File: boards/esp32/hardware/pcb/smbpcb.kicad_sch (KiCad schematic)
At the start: 61 parts, among them IC1 MiCS-6814, J1 USB_B_Micro, J2 PMS7003, Q1 SUD08P06-155L, SW1 RESET, SW2 RESET, U1 MCP73831-2-OT, U2 SGM6603-5.0YN6G_TR, U3 ESP32-WROOM-32, U4 SSD1306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

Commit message: moving stuff
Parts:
- added D2: LED_BLUE, Capacitor_SMD:C_0805_2012Metric, symbol Device:LED
- added D6: LED_GREEN, Capacitor_SMD:C_0805_2012Metric, symbol Device:LED
- added R11, R12: 1k5, symbol Device:R
- SW1, SW2: mfr_part_num ST-1102W-4.3 -> (none)
- U4: footprint mics:SSD1306_OLED-0.91-128x32 -> stuff:SSD1306_OLED-0.91-128x32
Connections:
- net GND: now also R11.1, R12.1
- net LED_GREEN: now reaches U3.30 (IO18)
- net LED_GREEN: now also D6.2 (A)
- net LED_BLUE: now reaches U3.31 (IO19)
- net LED_BLUE: now also D2.2 (A)
- new net: D2.1 (K), R11.2
- new net: D6.1 (K), R12.2
- no-connect marks 26 -> 24
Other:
- moved on the sheet: U6

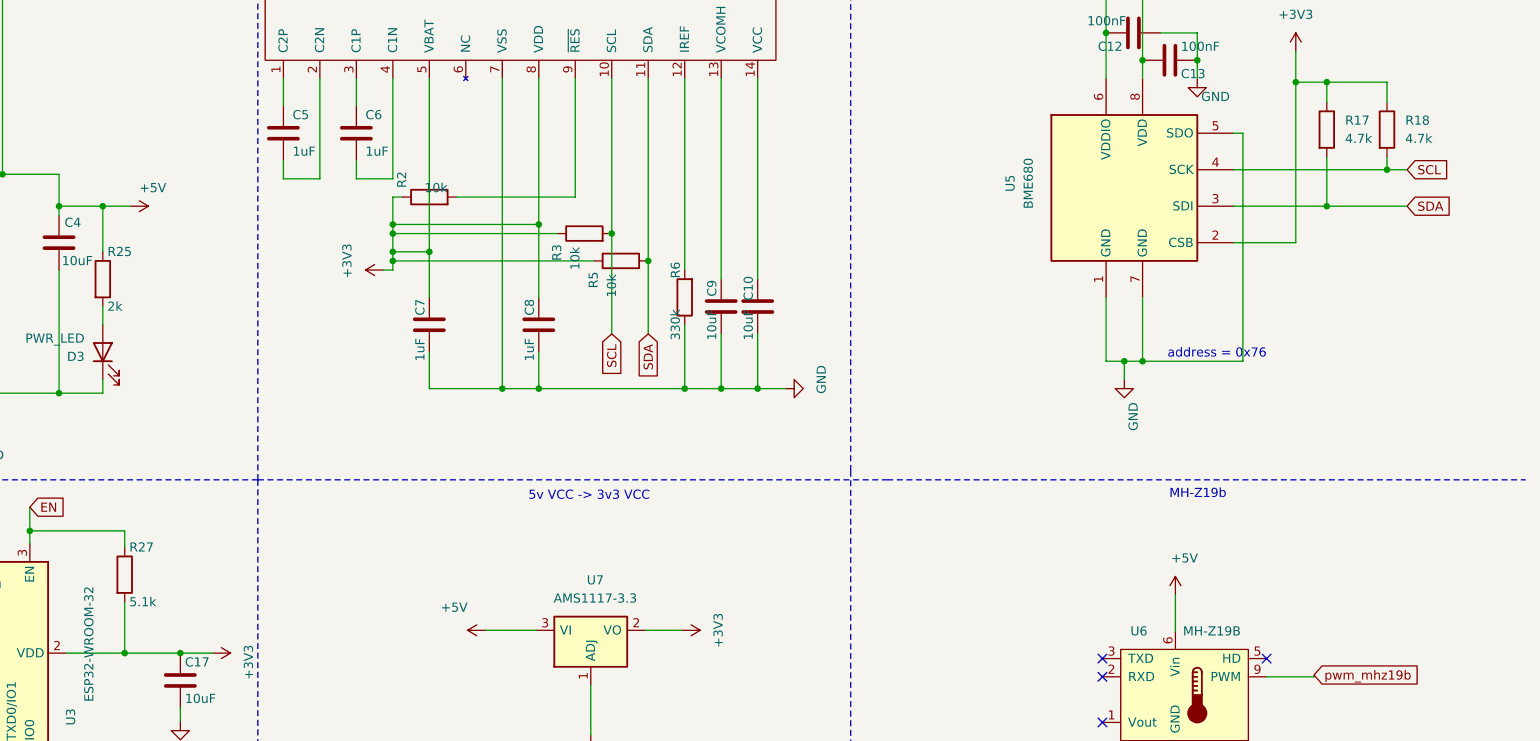
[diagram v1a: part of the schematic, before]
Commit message: added status leds
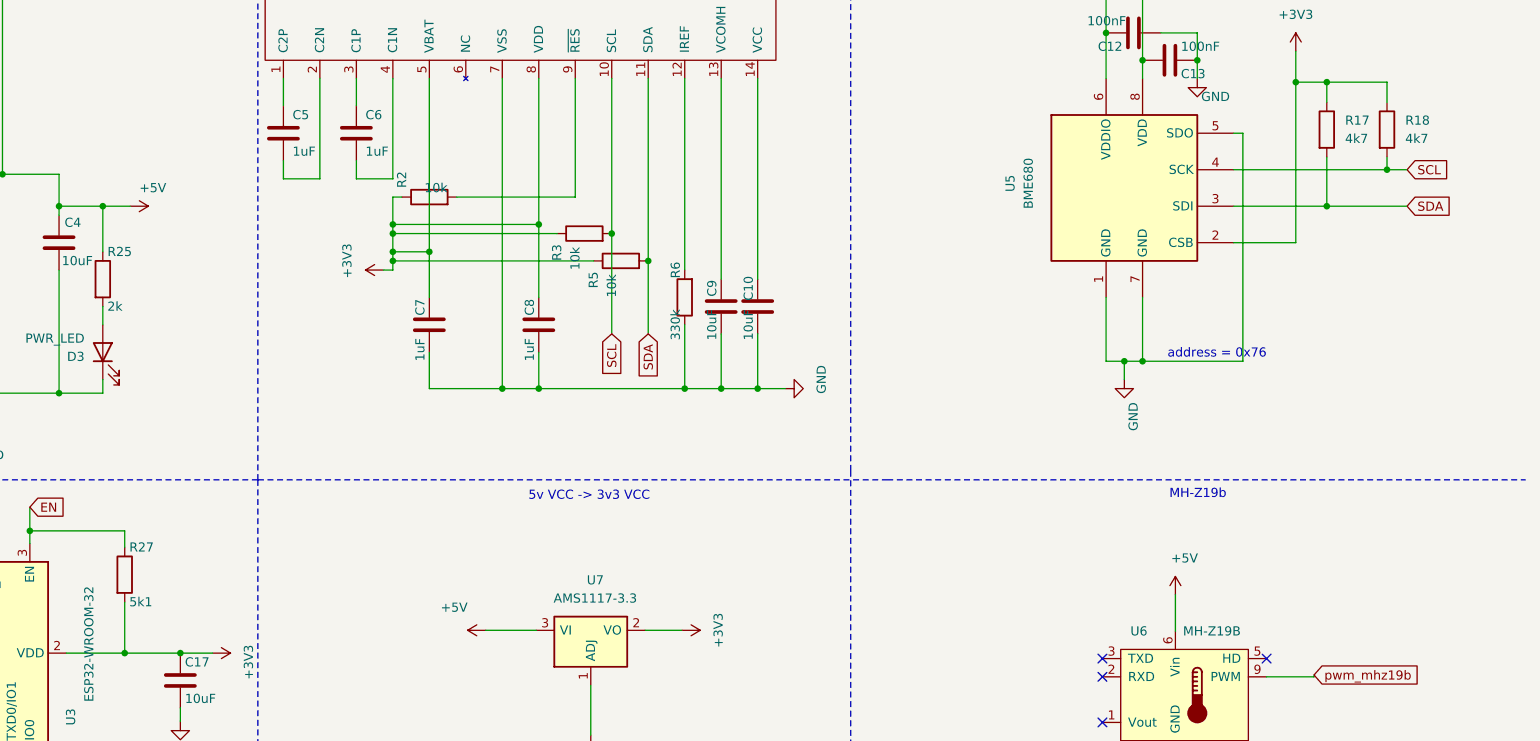
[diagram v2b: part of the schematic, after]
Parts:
- R11, R12: footprint (none) -> Capacitor_SMD:C_0805_2012Metric; LCSC (none) -> C203762; Mouser (none) -> CR0805-FX-1501ELF
- R17, R18: value 4.7k -> 4k7
- R27: value 5.1k -> 5k1
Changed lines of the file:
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@@
     (property "Reference" "R11" (id 0) (at 72.898 140.97 90))
     (property "Value" "1k5" (id 1) (at 71.247 137.922 90))
-    (property "Footprint" "" (id 2) (at 75.311 140.589 90)
+    (property "Footprint" "Capacitor_SMD:C_0805_2012Metric" (id 2) (at 75.311 140.589 90)
       (effects (font (size 1.27 1.27)) hide)
     )
     (property "Datasheet" "~" (id 3) (at 75.311 138.811 0)
+      (effects (font (size 1.27 1.27)) hide)
+    )
+    (property "LCSC" "C203762" (id 4) (at 75.311 138.811 0)
+      (effects (font (size 1.27 1.27)) hide)
+    )
+    (property "Mouser" "CR0805-FX-1501ELF" (id 5) (at 75.311 138.811 0)
       (effects (font (size 1.27 1.27)) hide)
     )
@@
     (property "Reference" "R12" (id 0) (at 73.025 143.764 90))
     (property "Value" "1k5" (id 1) (at 73.025 146.685 90))
-    (property "Footprint" "" (id 2) (at 76.581 146.812 90)
+    (property "Footprint" "Capacitor_SMD:C_0805_2012Metric" (id 2) (at 76.581 146.812 90)
       (effects (font (size 1.27 1.27)) hide)
     )
     (property "Datasheet" "~" (id 3) (at 76.581 145.034 0)
+      (effects (font (size 1.27 1.27)) hide)
+    )
+    (property "LCSC" "C203762" (id 4) (at 76.581 145.034 0)
+      (effects (font (size 1.27 1.27)) hide)
+    )
+    (property "Mouser" "CR0805-FX-1501ELF" (id 5) (at 76.581 145.034 0)
       (effects (font (size 1.27 1.27)) hide)
     )
@@
       (effects (font (size 1.27 1.27)) (justify left))
     )
-    (property "Value" "5.1k" (id 1) (at 215.773 113.538 0)
+    (property "Value" "5k1" (id 1) (at 215.773 113.538 0)
       (effects (font (size 1.27 1.27)) (justify left))
     )
@@
       (effects (font (size 1.27 1.27)) (justify left))
     )
-    (property "Value" "4.7k" (id 1) (at 385.064 49.022 0)
+    (property "Value" "4k7" (id 1) (at 385.064 49.022 0)
       (effects (font (size 1.27 1.27)) (justify left))
     )
@@
       (effects (font (size 1.27 1.27)) (justify left))
     )
-    (property "Value" "4.7k" (id 1) (at 393.446 49.022 0)
+    (property "Value" "4k7" (id 1) (at 393.446 49.022 0)
       (effects (font (size 1.27 1.27)) (justify left))
     )
@@
     )
     (path "/9ff0564e-254b-4e0a-9211-8ad0add8a40b"
-      (reference "R11") (unit 1) (value "1k5") (footprint "")
+      (reference "R11") (unit 1) (value "1k5") (footprint "Capacitor_SMD:C_0805_2012Metric")
     )
     (path "/3c9fc1fe-2257-4f43-ada5-ed1c4e4f94f3"
-      (reference "R12") (unit 1) (value "1k5") (footprint "")
+      (reference "R12") (unit 1) (value "1k5") (footprint "Capacitor_SMD:C_0805_2012Metric")
     )
     (path "/48ecb9b2-9c9c-42ac-9e9f-cab25ac716a7"
-      (reference "R17") (unit 1) (value "4.7k") (footprint "Capacitor_SMD:C_0805_2012Metric")
+      (reference "R17") (unit 1) (value "4k7") (footprint "Capacitor_SMD:C_0805_2012Metric")
     )
     (path "/33b47815-c87d-4054-811e-8a180ff4b4a5"
-      (reference "R18") (unit 1) (value "4.7k") (footprint "Capacitor_SMD:C_0805_2012Metric")
+      (reference "R18") (unit 1) (value "4k7") (footprint "Capacitor_SMD:C_0805_2012Metric")
     )
     (path "/0966f30f-63a6-408e-948c-ee9c9d9c86cb"
@@
     )
     (path "/7f6c1586-2cfd-4167-bcf0-c88517a26078"
-      (reference "R27") (unit 1) (value "5.1k") (footprint "Capacitor_SMD:C_0805_2012Metric")
+      (reference "R27") (unit 1) (value "5k1") (footprint "Capacitor_SMD:C_0805_2012Metric")
     )
     (path "/b69ae685-e389-4de0-86e5-81c4fbf5127d"

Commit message: changed some title block stuff
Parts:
- AUX_CONN1, AUX_CONN2, AUX_CONN3, AUX_CONN4: Mouser (none) -> 571-9-146278-0; mfr_part_num C124413 -> (none); notes (none) -> MOUSER MALE 40 pins per unit
- EXT_BATT1: Mouser (none) -> 801-87-040-10-001101; mfr_part_num C124375 -> (none); notes (none) -> MOUSER FEMALE 40 pins per unit
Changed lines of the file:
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@@
     (title "DiyAqi Esp32 Smb pcb")
     (date "2021-02-07")
-    (rev "v0.0.5")
+    (rev "v1.0.2")
     (company "Elam Day-Friedland")
   )
@@
       (effects (font (size 1.27 1.27)) hide)
     )
-    (property "mfr_part_num" "C124375" (id 4) (at 106.045 57.15 0)
+    (property "Mouser" "801-87-040-10-001101" (id 5) (at 106.045 57.15 0)
+      (effects (font (size 1.27 1.27)) hide)
+    )
+    (property "notes" "MOUSER FEMALE 40 pins per unit" (id 6) (at 106.045 57.15 0)
       (effects (font (size 1.27 1.27)) hide)
     )
@@
       (effects (font (size 1.27 1.27)) hide)
     )
-    (property "mfr_part_num" "C124413" (id 4) (at 41.91 109.22 0)
+    (property "Mouser" " 571-9-146278-0 " (id 5) (at 41.91 109.22 0)
+      (effects (font (size 1.27 1.27)) hide)
+    )
+    (property "notes" "MOUSER MALE 40 pins per unit" (id 6) (at 41.91 109.22 0)
       (effects (font (size 1.27 1.27)) hide)
     )
@@
       (effects (font (size 1.27 1.27)) hide)
     )
-    (property "mfr_part_num" "C124413" (id 4) (at 41.91 125.73 0)
+    (property "Mouser" " 571-9-146278-0 " (id 5) (at 41.91 125.73 0)
+      (effects (font (size 1.27 1.27)) hide)
+    )
+    (property "notes" "MOUSER MALE 40 pins per unit" (id 6) (at 41.91 125.73 0)
       (effects (font (size 1.27 1.27)) hide)
     )
@@
       (effects (font (size 1.27 1.27)) hide)
     )
-    (property "mfr_part_num" "C124413" (id 4) (at 85.09 108.585 0)
+    (property "Mouser" " 571-9-146278-0 " (id 5) (at 85.09 108.585 0)
+      (effects (font (size 1.27 1.27)) hide)
+    )
+    (property "notes" "MOUSER MALE 40 pins per unit" (id 6) (at 85.09 108.585 0)
       (effects (font (size 1.27 1.27)) hide)
     )
@@
       (effects (font (size 1.27 1.27)) hide)
     )
-    (property "mfr_part_num" "C124413" (id 4) (at 85.725 127.635 0)
+    (property "Mouser" " 571-9-146278-0 " (id 5) (at 85.725 127.635 0)
+      (effects (font (size 1.27 1.27)) hide)
+    )
+    (property "notes" "MOUSER MALE 40 pins per unit" (id 6) (at 85.725 127.635 0)
       (effects (font (size 1.27 1.27)) hide)
     )

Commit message: more readable schematic
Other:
- note added: "ESP32"
- note added: "PMS7003"
- note removed: "PMS7003 (logic is 3v3, 5V is only used for fan)"
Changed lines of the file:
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@@
   (title_block
     (title "DiyAqi Esp32 Smb pcb")
-    (date "2021-02-07")
+    (date "2021-03-20")
     (rev "v1.0.2")
     (company "Elam Day-Friedland")
@@
   )
   (polyline (pts (xy 10.16 96.52) (xy 10.16 97.79))
-    (stroke (width 0) (type dash) (color 0 0 0 0))
+    (stroke (width 1) (type dash) (color 0 0 0 0))
   )
   (polyline (pts (xy 10.16 152.4) (xy 124.46 152.4))
-    (stroke (width 0) (type dash) (color 0 0 0 0))
+    (stroke (width 1) (type dash) (color 0 0 0 0))
   )
   (polyline (pts (xy 124.46 152.4) (xy 124.46 96.52))
-    (stroke (width 0) (type dash) (color 0 0 0 0))
+    (stroke (width 1) (type dash) (color 0 0 0 0))
   )
   (polyline (pts (xy 124.46 152.4) (xy 124.46 218.44))
-    (stroke (width 0) (type dash) (color 0 0 0 0))
+    (stroke (width 1) (type dash) (color 0 0 0 0))
   )
   (polyline (pts (xy 124.46 218.44) (xy 233.68 218.44))
-    (stroke (width 0) (type dash) (color 0 0 0 0))
+    (stroke (width 1) (type dash) (color 0 0 0 0))
   )
   (polyline (pts (xy 233.68 10.16) (xy 233.68 96.52))
-    (stroke (width 0) (type dash) (color 0 0 0 0))
+    (stroke (width 1) (type dash) (color 0 0 0 0))
   )
   (polyline (pts (xy 233.68 96.52) (xy 10.16 96.52))
-    (stroke (width 0) (type dash) (color 0 0 0 0))
+    (stroke (width 1) (type dash) (color 0 0 0 0))
   )
   (polyline (pts (xy 233.68 96.52) (xy 233.68 152.4))
-    (stroke (width 0) (type dash) (color 0 0 0 0))
+    (stroke (width 1) (type dash) (color 0 0 0 0))
   )
   (polyline (pts (xy 233.68 96.52) (xy 321.31 96.52))
-    (stroke (width 0) (type dash) (color 0 0 0 0))
+    (stroke (width 1) (type dash) (color 0 0 0 0))
   )
   (polyline (pts (xy 233.68 152.4) (xy 124.46 152.4))
-    (stroke (width 0) (type dash) (color 0 0 0 0))
+    (stroke (width 1) (type dash) (color 0 0 0 0))
   )
   (polyline (pts (xy 233.68 152.4) (xy 316.23 152.4))
-    (stroke (width 0) (type dash) (color 0 0 0 0))
+    (stroke (width 1) (type dash) (color 0 0 0 0))
   )
   (polyline (pts (xy 233.68 218.44) (xy 233.68 152.4))
-    (stroke (width 0) (type dash) (color 0 0 0 0))
+    (stroke (width 1) (type dash) (color 0 0 0 0))
   )
   (polyline (pts (xy 285.75 152.4) (xy 285.75 218.44))
-    (stroke (width 0) (type dash) (color 0 0 0 0))
+    (stroke (width 1) (type dash) (color 0 0 0 0))
   )
   (polyline (pts (xy 285.75 218.44) (xy 410.21 218.44))
-    (stroke (width 0) (type dash) (color 0 0 0 0))
+    (stroke (width 1) (type dash) (color 0 0 0 0))
   )
   (polyline (pts (xy 286.385 218.44) (xy 233.68 218.44))
-    (stroke (width 0) (type dash) (color 0 0 0 0))
+    (stroke (width 1) (type dash) (color 0 0 0 0))
   )
   (polyline (pts (xy 316.23 8.89) (xy 316.23 95.25))
-    (stroke (width 0) (type dash) (color 0 0 0 0))
+    (stroke (width 1) (type dash) (color 0 0 0 0))
   )
   (polyline (pts (xy 316.23 95.25) (xy 316.23 152.4))
-    (stroke (width 0) (type dash) (color 0 0 0 0))
+    (stroke (width 1) (type dash) (color 0 0 0 0))
   )
   (polyline (pts (xy 316.23 152.4) (xy 410.21 152.4))
-    (stroke (width 0) (type dash) (color 0 0 0 0))
+    (stroke (width 1) (type dash) (color 0 0 0 0))
   )
   (polyline (pts (xy 321.31 96.52) (xy 410.21 96.52))
-    (stroke (width 0) (type dash) (color 0 0 0 0))
-  )
-  (text "2k resistor = 500mA charge current\n\n" (at 66.675 83.185 180)
-    (effects (font (size 1.27 1.27)) (justify right bottom))
-  )
-  (text "Auxillary Breakout Headers\n" (at 71.755 99.06 180)
-    (effects (font (size 1.27 1.27)) (justify right bottom))
-  )
-  (text "Battery Managment " (at 118.11 16.51 180)
-    (effects (font (size 1.27 1.27)) (justify right bottom))
-  )
-  (text "Flashing / Bootmode selection\n" (at 197.485 156.21 180)
-    (effects (font (size 1.27 1.27)) (justify right bottom))
+    (stroke (width 1) (type dash) (color 0 0 0 0))
+  )
+  (text "2k resistor = 500mA charge current\n\n" (at 68.58 72.771 180)
+    (effects (font (size 1 1)) (justify right bottom))
+  )
+  (text "Auxillary Breakout Headers\n" (at 96.647 103.124 180)
+    (effects (font (size 3 3)) (justify right bottom))
+  )
+  (text "Battery Managment " (at 118.237 18.415 180)
+    (effects (font (size 3 3)) (justify right bottom))
+  )
+  (text "ESP32\n" (at 177.546 103.505 180)
+    (effects (font (size 3 3)) (justify right bottom))
+  )
+  (text "Flashing / Bootmode selection\n" (at 214.757 157.861 180)
+    (effects (font (size 3 3)) (justify right bottom))
+  )
+  (text "PMS7003 \n\n\n" (at 273.05 169.418 180)
+    (effects (font (size 3 3)) (justify right bottom))
   )
   (text "OLED\n" (at 281.94 22.86 180)
-    (effects (font (size 1.27 1.27)) (justify right bottom))
-  )
-  (text "PMS7003 (logic is 3v3, 5V is only used for fan)\n" (at 283.21 156.21 180)
-    (effects (font (size 1.27 1.27)) (justify right bottom))
-  )
-  (text "5v VCC -> 3v3 VCC\n" (at 288.29 99.568 180)
-    (effects (font (size 1.27 1.27)) (justify right bottom))
-  )
-  (text "MiCS-6814\n" (at 363.22 156.21 180)
-    (effects (font (size 1.27 1.27)) (justify right bottom))
-  )
-  (text "MH-Z19b\n" (at 368.554 99.314 180)
-    (effects (font (size 1.27 1.27)) (justify right bottom))
+    (effects (font (size 3 3)) (justify right bottom))
+  )
+  (text "5v VCC -> 3v3 VCC\n" (at 300.736 106.553 180)
+    (effects (font (size 3 3)) (justify right bottom))
+  )
+  (text "MiCS-6814\n" (at 370.459 160.401 180)
+    (effects (font (size 3 3)) (justify right bottom))
   )
   (text "address = 0x76\n" (at 374.142 79.756 180)
-    (effects (font (size 1.27 1.27)) (justify right bottom))
-  )
-  (text "BME680\n" (at 375.92 16.51 180)
-    (effects (font (size 1.27 1.27)) (justify right bottom))
+    (effects (font (size 3 3)) (justify right bottom))
+  )
+  (text "MH-Z19b\n" (at 374.142 104.14 180)
+    (effects (font (size 3 3)) (justify right bottom))
+  )
+  (text "BME680\n" (at 377.063 18.923 180)
+    (effects (font (size 3 3)) (justify right bottom))
   )
   (global_label "ESP_TX1" (shape input) (at 31.75 106.68 180)

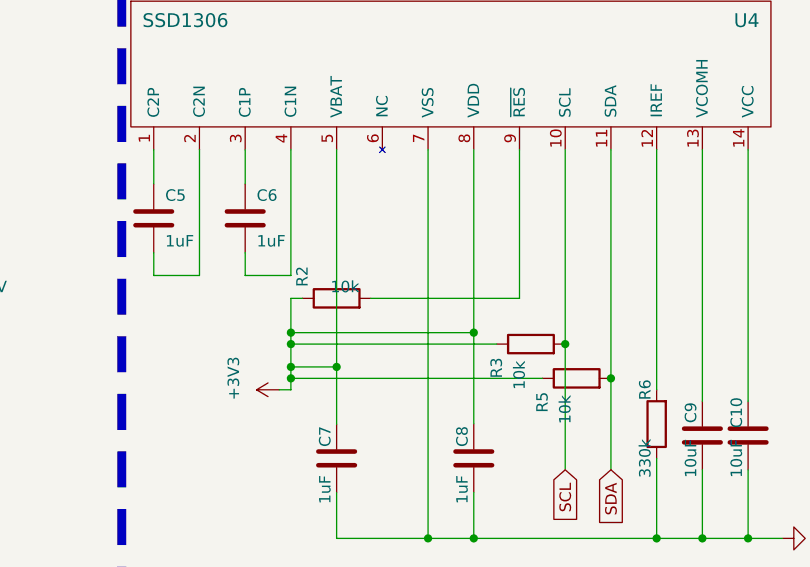
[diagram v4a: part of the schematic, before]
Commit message: removed oled reset pullup it broke the oled
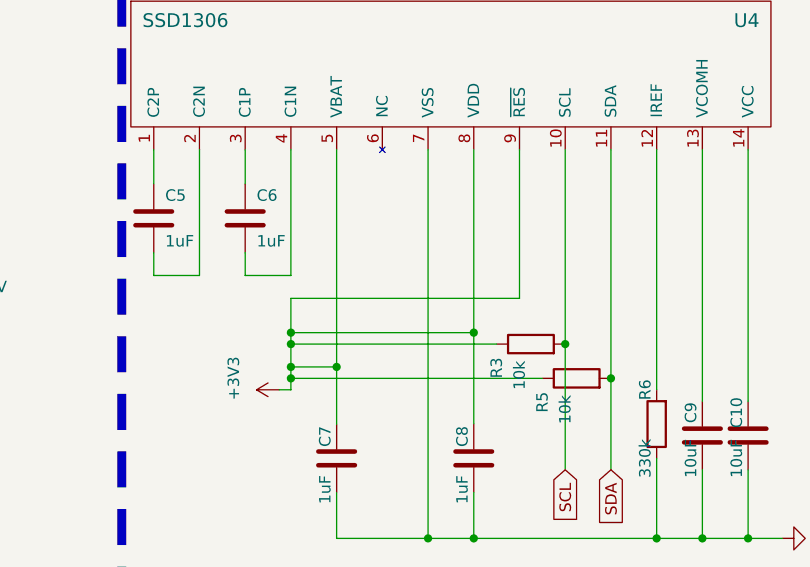
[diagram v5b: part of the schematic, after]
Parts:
- removed R2: 10k, Capacitor_SMD:C_0805_2012Metric, symbol Device:R
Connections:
- net +3V3: now also U4.9 (~RES)
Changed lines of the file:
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@@
     (stroke (width 0) (type solid) (color 0 0 0 0))
   )
-  (wire (pts (xy 252.476 57.15) (xy 253.746 57.15))
+  (wire (pts (xy 252.476 57.15) (xy 277.876 57.15))
     (stroke (width 0) (type solid) (color 0 0 0 0))
   )
@@
     (stroke (width 0) (type solid) (color 0 0 0 0))
   )
-  (wire (pts (xy 261.366 57.15) (xy 277.876 57.15))
-    (stroke (width 0) (type solid) (color 0 0 0 0))
-  )
   (wire (pts (xy 265.43 117.475) (xy 272.415 117.475))
     (stroke (width 0) (type solid) (color 0 0 0 0))
@@
     (pin "2")
   )
-  (symbol (lib_id "Device:R") (at 257.556 57.15 90) (unit 1)
-    (in_bom yes) (on_board yes)
-    (property "Reference" "R2" (id 0) (at 253.746 55.88 0)
-      (effects (font (size 1.27 1.27)) (justify left))
-    )
-    (property "Value" "10k" (id 1) (at 260.096 55.88 90)
-      (effects (font (size 1.27 1.27)) (justify left))
-    )
-    (property "Footprint" "Capacitor_SMD:C_0805_2012Metric" (id 2) (at 257.556 58.928 90)
-      (effects (font (size 1.27 1.27)) hide)
-    )
-    (property "Datasheet" "~" (id 3) (at 257.556 57.15 0)
-      (effects (font (size 1.27 1.27)) hide)
-    )
-    (property "LCSC" "C269724" (id 4) (at 257.556 57.15 0)
-      (effects (font (size 1.27 1.27)) hide)
-    )
-    (property "Mouser" " 71-TNPU080510K0AWEN " (id 5) (at 257.556 57.15 0)
-      (effects (font (size 1.27 1.27)) hide)
-    )
-    (pin "1")
-    (pin "2")
-  )
   (symbol (lib_id "Device:R") (at 279.146 62.23 90) (unit 1)
     (in_bom yes) (on_board yes)
@@
       (reference "R1") (unit 1) (value "2k") (footprint "Capacitor_SMD:C_0805_2012Metric")
     )
-    (path "/98de2776-dd77-4e8e-9c62-d0870f580a9f"
-      (reference "R2") (unit 1) (value "10k") (footprint "Capacitor_SMD:C_0805_2012Metric")
-    )
     (path "/b16dd033-20b0-4f39-9289-ebc5846f3ec0"
